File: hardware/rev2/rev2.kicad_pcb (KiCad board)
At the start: 2 copper layers, 72 x 80 mm, 34 parts, among them J1 Conn_01x09_Female, J2 RFM9X_header, J3 Conn_02x03_Odd_Even, U2 MPL3115A2, U3 Teensy3.6, U5 ADXL345BCCZ, U7 TPS2113ADRBR

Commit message: change silkscreen
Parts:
- D2, D3, D4, D5, D6, D7: footprint KingbrightLED:AA3528LSECKT-J4 -> rev2_lib:AA3528LSECKT-J4
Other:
- board text added: "Olin Rocketry Rev 2 4/9/2021 Ian Eykamp"
- board text removed: "Olin Rocketry Rev 1 1/25/2021 Ian Eykamp"

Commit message: finesse traces
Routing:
- added copper zone on B.Cu, net GND
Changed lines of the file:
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@@
   (segment (start 163.6549 107.1679) (end 163.6549 105.2041) (width 0.25) (layer F.Cu) (net 6) (status 400010))
   (segment (start 163.6549 105.2041) (end 166.243 102.616) (width 0.25) (layer F.Cu) (net 6) (status 800020))
-  (segment (start 162.56 82.296) (end 164.846 84.582) (width 0.25) (layer F.Cu) (net 26) (status 400010))
-  (segment (start 168.529 84.582) (end 171.323 87.376) (width 0.25) (layer F.Cu) (net 26) (status 800020))
-  (segment (start 164.846 84.582) (end 168.529 84.582) (width 0.25) (layer F.Cu) (net 26))
+  (segment (start 162.56 82.296) (end 165.346 85.082) (width 0.25) (layer F.Cu) (net 26) (status 400000))
+  (segment (start 169.029 85.082) (end 171.323 87.376) (width 0.25) (layer F.Cu) (net 26) (status 800000))
+  (segment (start 165.346 85.082) (end 169.029 85.082) (width 0.25) (layer F.Cu) (net 26))
   (segment (start 165.1 82.296) (end 166.878 84.074) (width 0.25) (layer F.Cu) (net 27) (status 400010))
   (segment (start 170.561 84.074) (end 173.863 87.376) (width 0.25) (layer F.Cu) (net 27) (status 800020))
@@
   (segment (start 121.89968 105.26268) (end 128.27 111.633) (width 0.4) (layer B.Cu) (net 54) (status 800020))
   (segment (start 121.5644 105.26268) (end 121.89968 105.26268) (width 0.4) (layer B.Cu) (net 54))
-  (segment (start 166.243 87.376) (end 164.211 85.344) (width 0.4) (layer B.Cu) (net 55) (status 400010))
+  (segment (start 166.243 87.376) (end 164.411 85.544) (width 0.4) (layer B.Cu) (net 55) (status 400010))
   (segment (start 145.45 52.2) (end 145.45 52) (width 0.4) (layer F.Cu) (net 55) (status C00000))
   (segment (start 147.75 54.75) (end 145.325 52.325) (width 0.4) (layer F.Cu) (net 55))
@@
   (segment (start 147.8096 55.3096) (end 147.75 55.25) (width 0.4) (layer B.Cu) (net 55))
   (via (at 147.75 55.25) (size 0.8) (drill 0.4) (layers F.Cu B.Cu) (net 55))
-  (segment (start 152.146 85.344) (end 149.86 83.058) (width 0.4) (layer B.Cu) (net 55))
-  (segment (start 164.211 85.344) (end 152.146 85.344) (width 0.4) (layer B.Cu) (net 55))
+  (segment (start 152.346 85.544) (end 149.86 83.058) (width 0.4) (layer B.Cu) (net 55))
+  (segment (start 164.411 85.544) (end 152.346 85.544) (width 0.4) (layer B.Cu) (net 55))
   (segment (start 147.8096 81.0076) (end 147.8096 65) (width 0.4) (layer B.Cu) (net 55))
   (segment (start 147.8096 65) (end 147.8096 62.5) (width 0.4) (layer B.Cu) (net 55))
@@
     (connect_pads (clearance 0.25))
     (min_thickness 0.24)
+    (fill yes (arc_segments 32) (thermal_gap 0.508) (thermal_bridge_width 0.508))
+    (polygon
+      (pts
+        (xy 104 36.75) (xy 177 36.75) (xy 177 117.75) (xy 104.25 117.75)
+      )
+    )
+  )
+  (zone (net 1) (net_name GND) (layer B.Cu) (hatch edge 0.508)
+    (connect_pads (clearance 0.25))
+    (min_thickness 0.24)

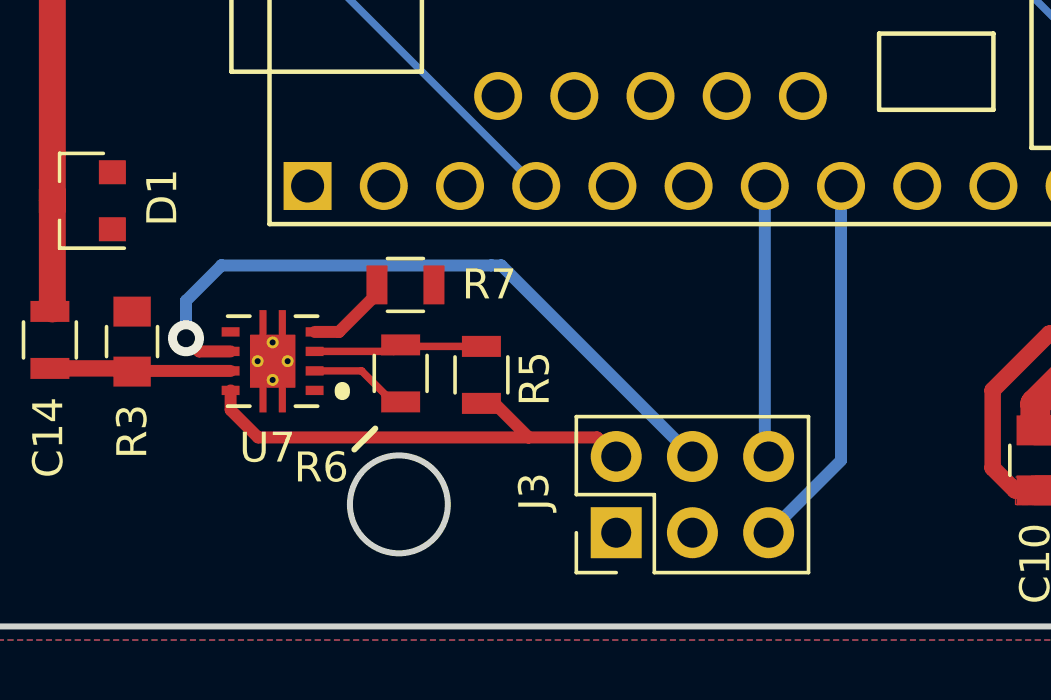
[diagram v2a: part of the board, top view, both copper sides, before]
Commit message: add Molex Connector to layout
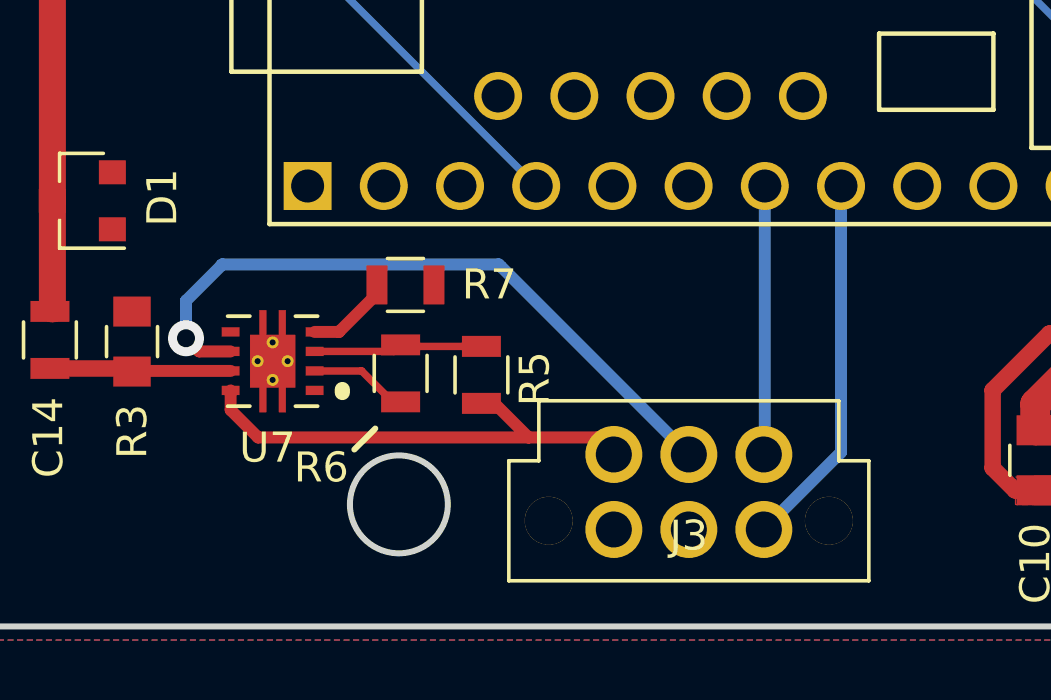
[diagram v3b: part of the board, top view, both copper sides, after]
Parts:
- J3: footprint Connector_PinHeader_2.54mm:PinHeader_2x03_P2.54mm_Vertical -> footprints:Molex_Nano-Fit_105312-1106
- moved J3 2.45 mm to (128.2, 113.8), turned to 0 degrees
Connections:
- J3 pad 2: 3.3VBMS -> Net-(J3-Pad2)
- J3 pad 3: Net-(J3-Pad3) -> DROGUE_DEPLOY
- J3 pad 4: 3.3VBMS_Backup -> 3.3VBMS
- J3 pad 5: DROGUE_DEPLOY -> 3.3VBMS_Backup

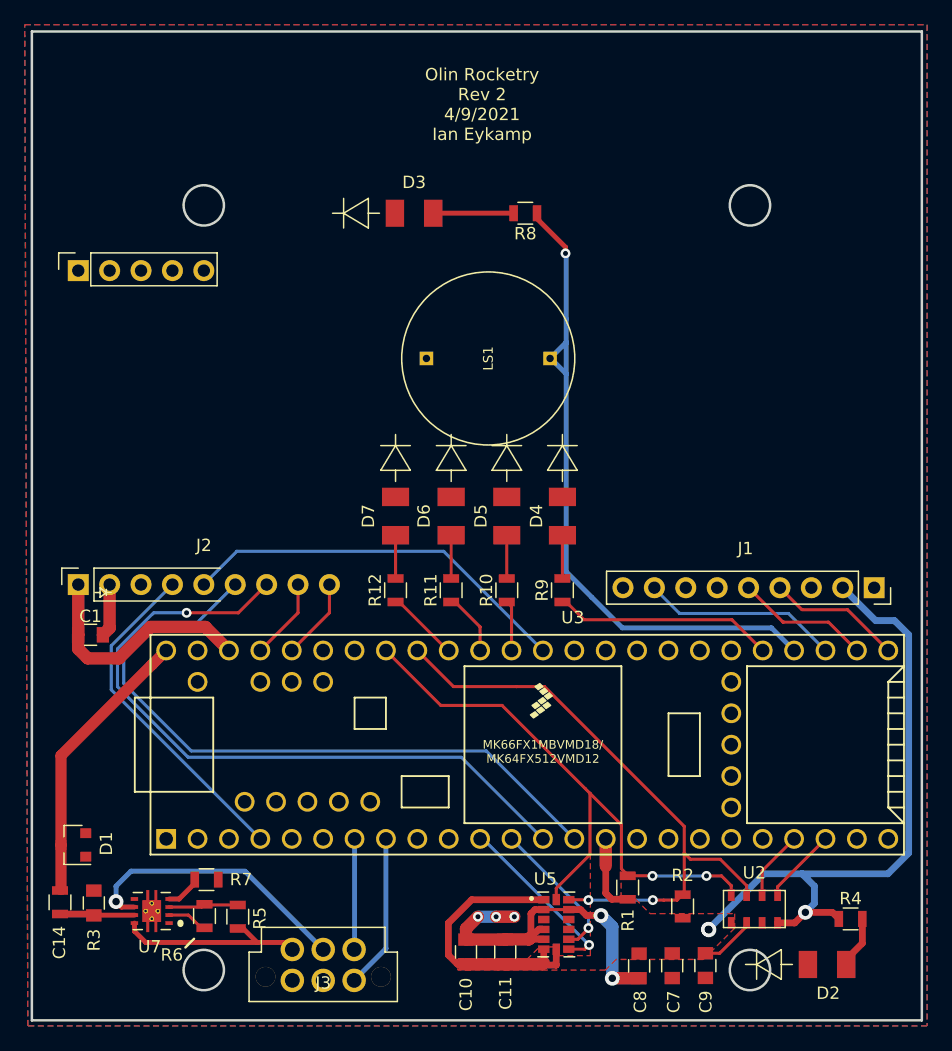
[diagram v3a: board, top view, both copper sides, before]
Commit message: add vias galore
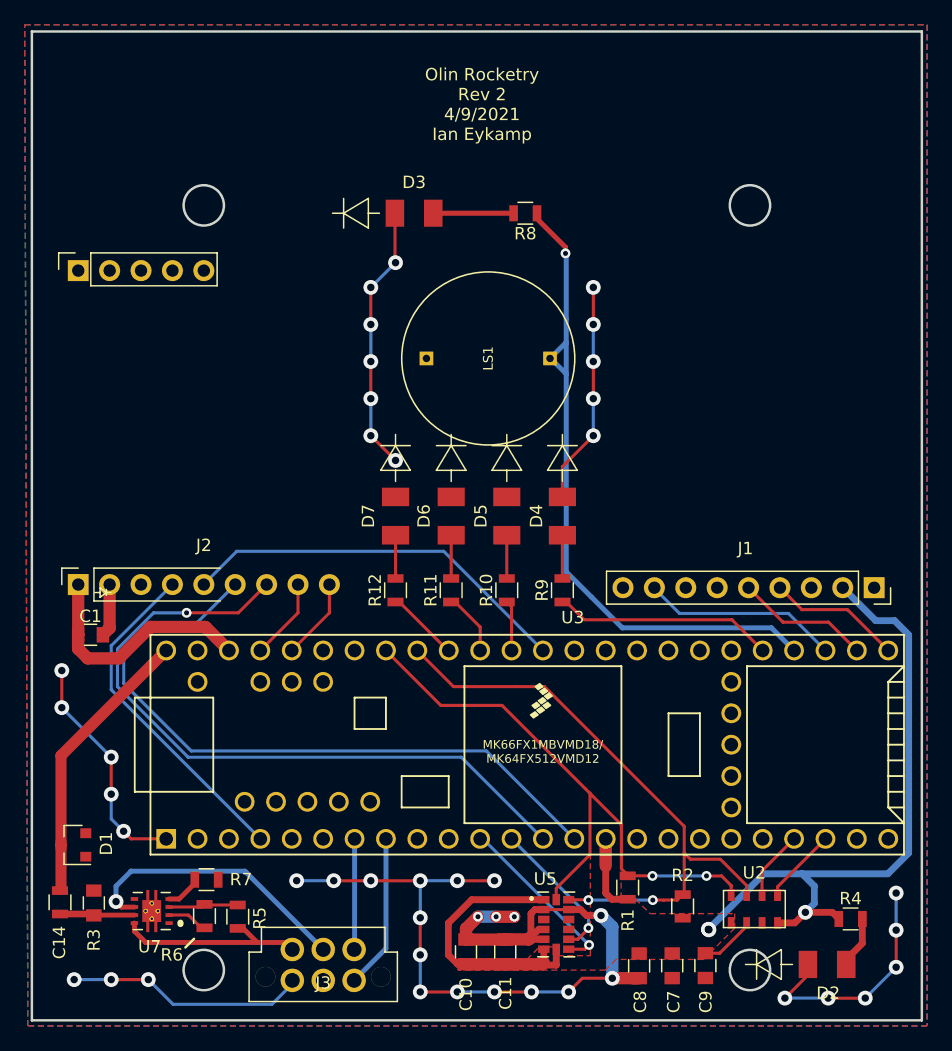
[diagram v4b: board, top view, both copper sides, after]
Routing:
- net GND: track 40.5 -> 178.9 mm, vias 5 -> 44
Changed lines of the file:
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@@
     (thickness 1.6)
     (drawings 20)
-    (tracks 257)
+    (tracks 344)
     (zones 0)
     (modules 34)
@@
   )
   (setup
-    (last_trace_width 0.4)
+    (last_trace_width 0.25)
     (user_trace_width 0.4)
     (user_trace_width 0.475)
@@
   (segment (start 110.871 82.042) (end 110.871 85.5566) (width 1) (layer F.Cu) (net 1) (status 400010))
   (segment (start 110.871 85.5566) (end 110.3216 86.106) (width 1) (layer F.Cu) (net 1) (status 800020))
+  (via (at 126 106) (size 1.2) (drill 0.6) (layers F.Cu B.Cu) (net 1))
+  (segment (start 129 106) (end 126 106) (width 0.25) (layer B.Cu) (net 1))
+  (via (at 129 106) (size 1.2) (drill 0.6) (layers F.Cu B.Cu) (net 1))
+  (segment (start 132 106) (end 129 106) (width 0.25) (layer F.Cu) (net 1))
+  (via (at 136 106) (size 1.2) (drill 0.6) (layers F.Cu B.Cu) (net 1))
+  (segment (start 136 106) (end 136 109) (width 0.25) (layer B.Cu) (net 1))
+  (segment (start 149.1064 113.8936) (end 148 115) (width 0.25) (layer F.Cu) (net 1))
+  (segment (start 149.1064 113.8936) (end 151.5364 113.8936) (width 0.25) (layer F.Cu) (net 1))
+  (segment (start 136 112) (end 136 115) (width 0.25) (layer B.Cu) (net 1))
+  (via (at 148 115) (size 1.2) (drill 0.6) (layers F.Cu B.Cu) (net 1))
+  (segment (start 148 115) (end 145 115) (width 0.25) (layer B.Cu) (net 1))
+  (via (at 145 115) (size 1.2) (drill 0.6) (layers F.Cu B.Cu) (net 1))
+  (segment (start 145 115) (end 142 115) (width 0.25) (layer F.Cu) (net 1))
+  (via (at 142 115) (size 1.2) (drill 0.6) (layers F.Cu B.Cu) (net 1))
+  (segment (start 142 115) (end 139 115) (width 0.25) (layer B.Cu) (net 1))
+  (via (at 139 115) (size 1.2) (drill 0.6) (layers F.Cu B.Cu) (net 1))
+  (segment (start 139 115) (end 136 115) (width 0.25) (layer F.Cu) (net 1))
+  (via (at 136 115) (size 1.2) (drill 0.6) (layers F.Cu B.Cu) (net 1))
+  (via (at 136 112) (size 1.2) (drill 0.6) (layers F.Cu B.Cu) (net 1))
+  (segment (start 136 112) (end 136 109) (width 0.25) (layer F.Cu) (net 1))
+  (via (at 136 109) (size 1.2) (drill 0.6) (layers F.Cu B.Cu) (net 1))
+  (segment (start 136 106) (end 132 106) (width 0.25) (layer F.Cu) (net 1))
+  (via (at 132 106) (size 1.2) (drill 0.6) (layers F.Cu B.Cu) (net 1))
+  (segment (start 136 106) (end 139 106) (width 0.25) (layer B.Cu) (net 1))
+  (via (at 142 106) (size 1.2) (drill 0.6) (layers F.Cu B.Cu) (net 1))
+  (segment (start 139 106) (end 142 106) (width 0.25) (layer F.Cu) (net 1))
+  (via (at 139 106) (size 1.2) (drill 0.6) (layers F.Cu B.Cu) (net 1))
+  (segment (start 125.65 114.065) (end 125.65 114.35) (width 0.25) (layer B.Cu) (net 1) (status C00000))
+  (via (at 108 114) (size 1.2) (drill 0.6) (layers F.Cu B.Cu) (net 1))
+  (segment (start 111 114) (end 108 114) (width 0.25) (layer B.Cu) (net 1))
+  (via (at 111 114) (size 1.2) (drill 0.6) (layers F.Cu B.Cu) (net 1))
+  (segment (start 114 114) (end 111 114) (width 0.25) (layer F.Cu) (net 1))
+  (via (at 114 114) (size 1.2) (drill 0.6) (layers F.Cu B.Cu) (net 1))
+  (segment (start 116 116) (end 114 114) (width 0.25) (layer B.Cu) (net 1))
+  (segment (start 124 116) (end 116 116) (width 0.25) (layer B.Cu) (net 1))
+  (segment (start 125.65 114.35) (end 124 116) (width 0.25) (layer B.Cu) (net 1) (status 400000))
+  (segment (start 115.443 102.616) (end 112.616 102.616) (width 0.25) (layer F.Cu) (net 1) (status 400000))
+  (segment (start 112.616 102.616) (end 112 102) (width 0.25) (layer F.Cu) (net 1))
+  (via (at 112 102) (size 1.2) (drill 0.6) (layers F.Cu B.Cu) (net 1))
+  (segment (start 112 102) (end 111 101) (width 0.25) (layer B.Cu) (net 1))
+  (segment (start 111 101) (end 111 99) (width 0.25) (layer B.Cu) (net 1))
+  (via (at 111 99) (size 1.2) (drill 0.6) (layers F.Cu B.Cu) (net 1))
+  (segment (start 111 99) (end 111 96) (width 0.25) (layer F.Cu) (net 1))
+  (via (at 111 96) (size 1.2) (drill 0.6) (layers F.Cu B.Cu) (net 1))
+  (segment (start 111 96) (end 107 92) (width 0.25) (layer B.Cu) (net 1))
+  (via (at 107 92) (size 1.2) (drill 0.6) (layers F.Cu B.Cu) (net 1))
+  (segment (start 107 92) (end 107 89) (width 0.25) (layer F.Cu) (net 1))
+  (via (at 107 89) (size 1.2) (drill 0.6) (layers F.Cu B.Cu) (net 1))
+  (segment (start 167.36 112.776) (end 167.36 113.64) (width 0.25) (layer F.Cu) (net 1) (status C00000))
+  (via (at 174.5 107) (size 1.2) (drill 0.6) (layers F.Cu B.Cu) (net 1))
+  (segment (start 174.5 110) (end 174.5 107) (width 0.25) (layer B.Cu) (net 1))
+  (via (at 174.5 110) (size 1.2) (drill 0.6) (layers F.Cu B.Cu) (net 1))
+  (segment (start 174.5 113) (end 174.5 110) (width 0.25) (layer F.Cu) (net 1))
+  (via (at 174.5 113) (size 1.2) (drill 0.6) (layers F.Cu B.Cu) (net 1))
+  (segment (start 172 115.5) (end 174.5 113) (width 0.25) (layer B.Cu) (net 1))
+  (via (at 172 115.5) (size 1.2) (drill 0.6) (layers F.Cu B.Cu) (net 1))
+  (segment (start 169 115.5) (end 172 115.5) (width 0.25) (layer F.Cu) (net 1))
+  (via (at 169 115.5) (size 1.2) (drill 0.6) (layers F.Cu B.Cu) (net 1))
+  (segment (start 165.5 115.5) (end 169 115.5) (width 0.25) (layer B.Cu) (net 1))
+  (segment (start 167.36 113.64) (end 165.5 115.5) (width 0.25) (layer F.Cu) (net 1) (status 400000))
+  (via (at 165.5 115.5) (size 1.2) (drill 0.6) (layers F.Cu B.Cu) (net 1))
+  (segment (start 133.95 52) (end 133.95 55.95) (width 0.25) (layer F.Cu) (net 1) (status 400000))
+  (via (at 134 72) (size 1.2) (drill 0.6) (layers F.Cu B.Cu) (net 1))
+  (segment (start 132 70) (end 134 72) (width 0.25) (layer F.Cu) (net 1))
+  (via (at 132 70) (size 1.2) (drill 0.6) (layers F.Cu B.Cu) (net 1))
+  (segment (start 132 67) (end 132 70) (width 0.25) (layer B.Cu) (net 1))
+  (via (at 132 67) (size 1.2) (drill 0.6) (layers F.Cu B.Cu) (net 1))
+  (segment (start 132 64) (end 132 67) (width 0.25) (layer F.Cu) (net 1))
+  (via (at 132 64) (size 1.2) (drill 0.6) (layers F.Cu B.Cu) (net 1))
+  (segment (start 132 61) (end 132 64) (width 0.25) (layer B.Cu) (net 1))
+  (via (at 132 61) (size 1.2) (drill 0.6) (layers F.Cu B.Cu) (net 1))
+  (segment (start 132 58) (end 132 61) (width 0.25) (layer F.Cu) (net 1))
+  (via (at 132 58) (size 1.2) (drill 0.6) (layers F.Cu B.Cu) (net 1))
+  (segment (start 134 56) (end 132 58) (width 0.25) (layer B.Cu) (net 1))
+  (via (at 134 56) (size 1.2) (drill 0.6) (layers F.Cu B.Cu) (net 1))
+  (segment (start 133.95 55.95) (end 134 56) (width 0.25) (layer F.Cu) (net 1))
+  (segment (start 147.5 74.95) (end 147.5 72.5) (width 0.25) (layer F.Cu) (net 1) (status 400000))
+  (via (at 150 58) (size 1.2) (drill 0.6) (layers F.Cu B.Cu) (net 1))
+  (segment (start 150 61) (end 150 58) (width 0.25) (layer F.Cu) (net 1))
+  (via (at 150 61) (size 1.2) (drill 0.6) (layers F.Cu B.Cu) (net 1))
+  (segment (start 150 64) (end 150 61) (width 0.25) (layer B.Cu) (net 1))
+  (via (at 150 64) (size 1.2) (drill 0.6) (layers F.Cu B.Cu) (net 1))
+  (segment (start 150 67) (end 150 64) (width 0.25) (layer F.Cu) (net 1))
+  (via (at 150 67) (size 1.2) (drill 0.6) (layers F.Cu B.Cu) (net 1))
+  (segment (start 150 70) (end 150 67) (width 0.25) (layer B.Cu) (net 1))
+  (via (at 150 70) (size 1.2) (drill 0.6) (layers F.Cu B.Cu) (net 1))
+  (segment (start 147.5 72.5) (end 150 70) (width 0.25) (layer F.Cu) (net 1))
   (segment (start 159.06496 111.86744) (end 160.22244 111.86744) (width 0.25) (layer F.Cu) (net 2) (status 400010))
   (segment (start 162.4049 109.68498) (end 162.4049 109.4179) (width 0.25) (layer F.Cu) (net 2) (status C00030))
